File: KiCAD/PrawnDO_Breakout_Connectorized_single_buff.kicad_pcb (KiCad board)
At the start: 2 copper layers, 154.4 x 84.1 mm, 62 parts, among them IC1 74LVT245D,118, IC2 74LVT245D,118, IC3 74LVT245D,118, IC4 74LVT245D,118, J1 do15, J10 do6, J11 do5, J12 do4, J13 do3, J14 do2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

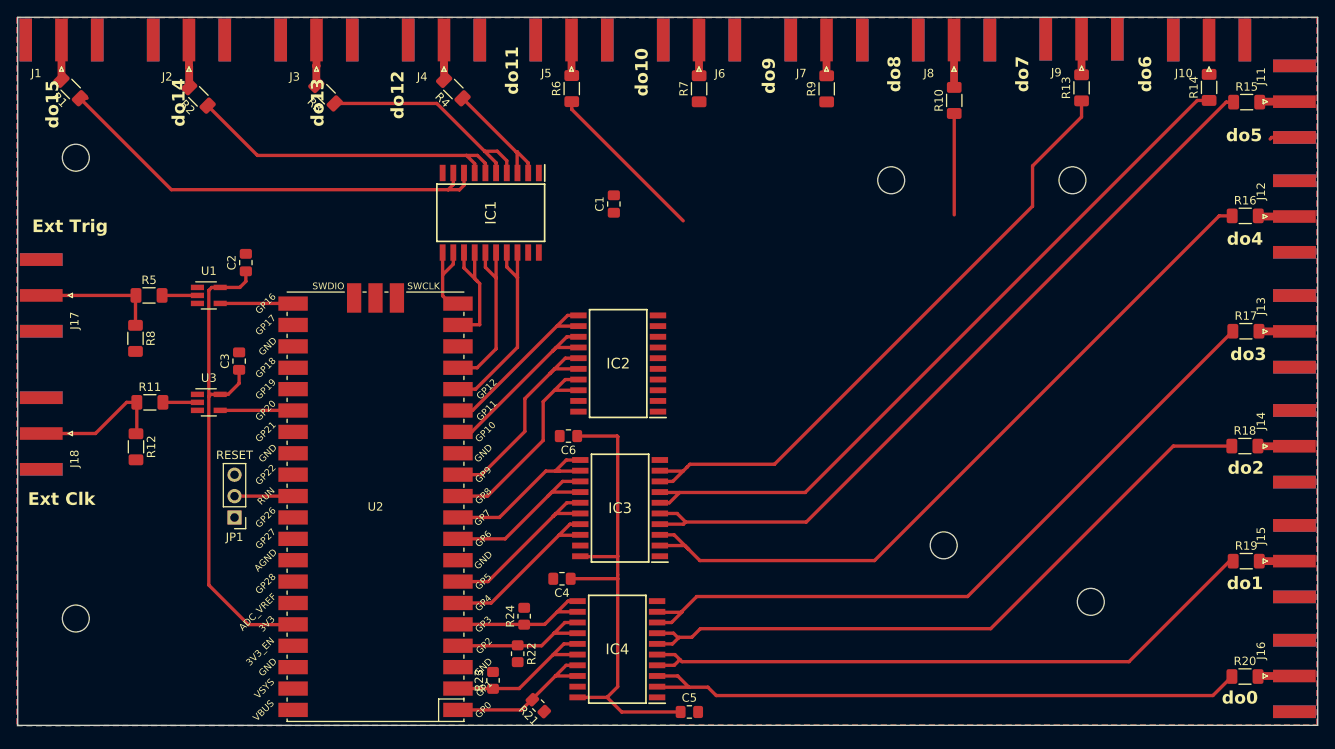
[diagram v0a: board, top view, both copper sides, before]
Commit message: Made changes to layout of board and added components
Schematic needs tidying up
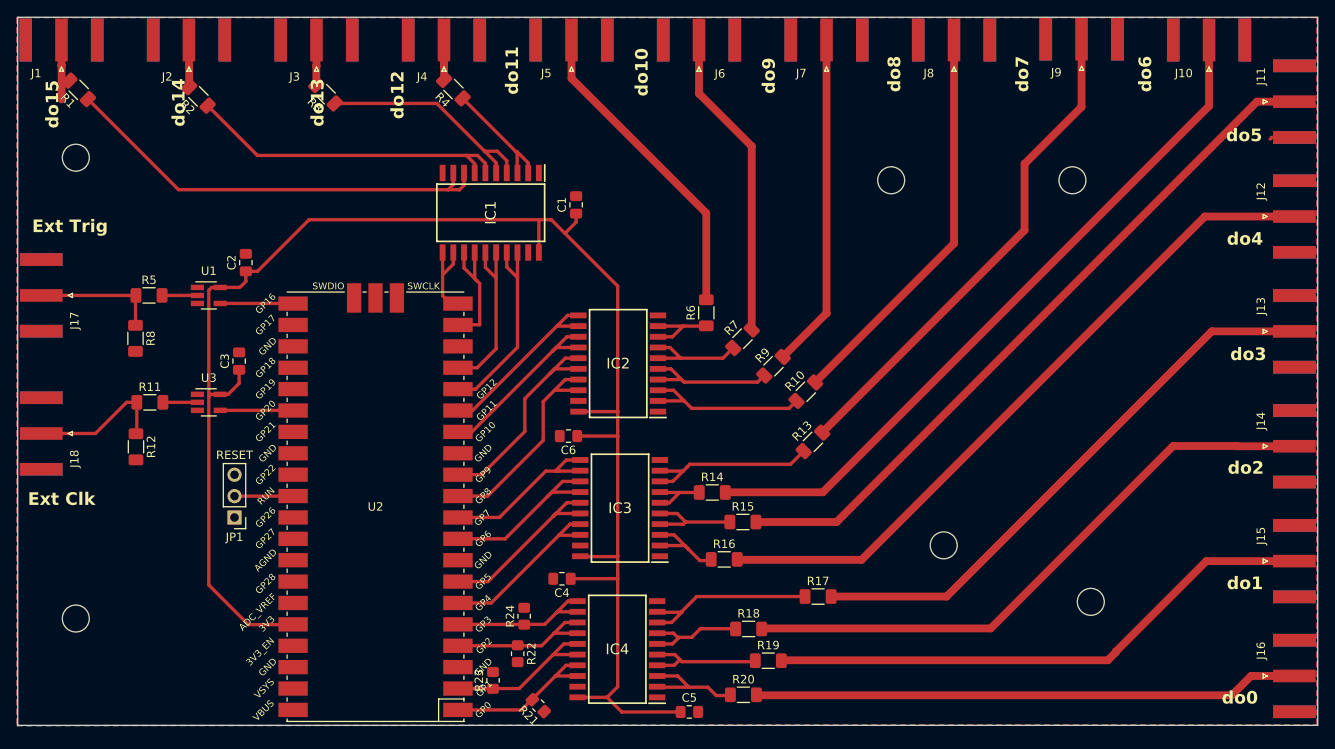
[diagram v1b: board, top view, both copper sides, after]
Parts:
- moved R15 77.9 mm to (154.0, 114.2)
- moved R14 76.1 mm to (150.4, 110.6), turned to 0 degrees
- moved R16 74.1 mm to (151.8, 118.6)
- moved R18 62.8 mm to (154.7, 126.8)
- moved R17 59.8 mm to (163.0, 123.0)
- moved R20 59.6 mm to (154.1, 134.7)
- moved R19 58.0 mm to (157.1, 130.6)
- moved R13 52.8 mm to (162.3, 104.6), turned to 45 degrees
- moved R10 38.8 mm to (161.5, 98.7), turned to 45 degrees
- moved R9 33.5 mm to (157.7, 95.6), turned to 45 degrees
- moved R6 31.1 mm to (149.7, 89.3)
- moved R7 30.1 mm to (154.0, 92.4), turned to 45 degrees
- moved C1 4.48 mm to (134.2, 76.5)
- moved R1 0.96 mm to (75.1, 62.8)
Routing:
- net do6: track 0.00 -> 84.3 mm
- net Net-(IC3-A2): track 92.4 -> 11.9 mm
- net do5: track 4.15 -> 84.6 mm
- net Net-(IC3-A4): track 87.4 -> 7.53 mm
- net 3_3V_Pico: track 119.1 -> 198.5 mm
- net Net-(IC3-A0): track 89.8 -> 11.0 mm
- net do4: track 4.32 -> 83.1 mm
- net do2: track 4.31 -> 72.3 mm
- net Net-(IC4-A4): track 80.7 -> 12.8 mm
- net Net-(IC4-A6): track 85.7 -> 21.9 mm
- net do3: track 4.22 -> 68.1 mm
- net do1: track 4.17 -> 65.9 mm
- net Net-(IC4-A2): track 76.7 -> 15.0 mm
- net do0: track 4.35 -> 64.9 mm
- net Net-(IC4-A0): track 74.0 -> 13.5 mm
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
